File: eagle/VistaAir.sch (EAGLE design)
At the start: 10 parts

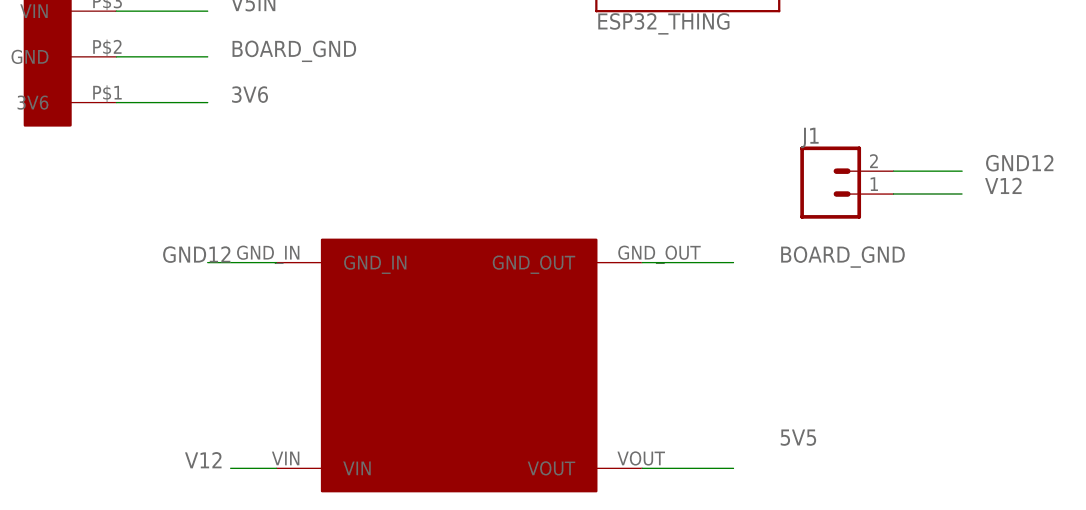
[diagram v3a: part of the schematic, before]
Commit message: proper stable power supply on board with buck converter into liner regulators
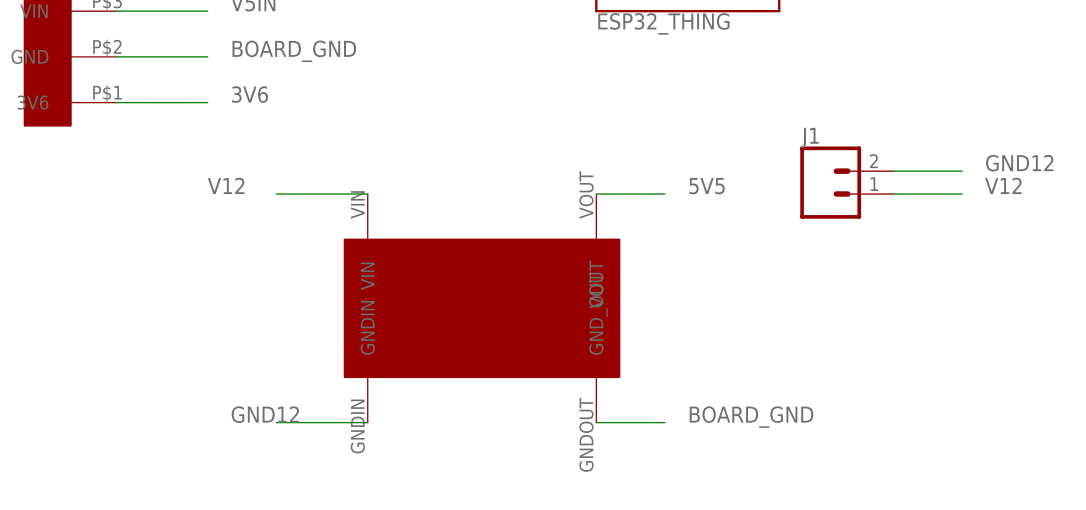
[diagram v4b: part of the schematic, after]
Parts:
- U$2: value MP1584EN_STEPDOWN_MODULE -> LM2596_STEPDOWN_MODULE; device kevins_parts:MP1584EN_STEPDOWN_MODULE -> kevins_parts:LM2596_STEPDOWN_MODULE
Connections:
- net GND12: now also U$2.GNDIN; no longer U$2.GND_IN
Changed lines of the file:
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@@
 <part name="C2" library="adafruit" deviceset="CPOL-US" device="TT5D10" value="330mu"/>
 <part name="C1" library="adafruit" deviceset="CPOL-US" device="TT2D5" value="10mu"/>
-<part name="U$2" library="kevins_parts" deviceset="MP1584EN_STEPDOWN_MODULE" device=""/>
+<part name="U$2" library="kevins_parts" deviceset="LM2596_STEPDOWN_MODULE" device=""/>
 </parts>
 <sheets>
@@
 <instance part="C2" gate="G$1" x="25.4" y="7.62"/>
 <instance part="C1" gate="G$1" x="25.4" y="40.64"/>
-<instance part="U$2" gate="G$1" x="101.6" y="-7.62"/>
+<instance part="U$2" gate="G$1" x="99.06" y="-27.94" rot="R270"/>
 </instances>
 <busses>
@@
 </segment>
 <segment>
-<pinref part="U$2" gate="G$1" pin="GND_OUT"/>
-<wire x1="121.92" y1="5.08" x2="132.08" y2="5.08" width="0.1524" layer="91"/>
-<label x="137.16" y="5.08" size="1.778" layer="95"/>
-</segment>
-<segment>
 <pinref part="L7805" gate="J$1" pin="2"/>
 <wire x1="20.32" y1="22.86" x2="25.4" y2="22.86" width="0.1524" layer="91"/>
 <label x="27.94" y="22.86" size="1.778" layer="95"/>
 </segment>
+<segment>
+<pinref part="U$2" gate="G$1" pin="GND_OUT"/>
+<wire x1="116.84" y1="-12.7" x2="124.46" y2="-12.7" width="0.1524" layer="91"/>
+<label x="127" y="-12.7" size="1.778" layer="95"/>
+</segment>
 </net>
 <net name="ENC2B" class="0">
@@
 <segment>
 <pinref part="U$2" gate="G$1" pin="VIN"/>
-<wire x1="81.28" y1="-17.78" x2="76.2" y2="-17.78" width="0.1524" layer="91"/>
-<label x="71.12" y="-17.78" size="1.778" layer="95"/>
+<wire x1="91.44" y1="12.7" x2="81.28" y2="12.7" width="0.1524" layer="91"/>
+<label x="73.66" y="12.7" size="1.778" layer="95"/>
 </segment>
 </net>
@@
 </segment>
 <segment>
-<pinref part="U$2" gate="G$1" pin="GND_IN"/>
-<wire x1="81.28" y1="5.08" x2="73.66" y2="5.08" width="0.1524" layer="91"/>
-<label x="68.58" y="5.08" size="1.778" layer="95"/>
+<pinref part="U$2" gate="G$1" pin="GNDIN"/>
+<wire x1="91.44" y1="-12.7" x2="81.28" y2="-12.7" width="0.1524" layer="91"/>
+<label x="76.2" y="-12.7" size="1.778" layer="95"/>
 </segment>
 </net>
@@
 </segment>
 <segment>
-<pinref part="U$2" gate="G$1" pin="VOUT"/>
-<wire x1="121.92" y1="-17.78" x2="132.08" y2="-17.78" width="0.1524" layer="91"/>
-<label x="137.16" y="-15.24" size="1.778" layer="95"/>
-</segment>
-<segment>
 <pinref part="L7805" gate="J$1" pin="1"/>
 <wire x1="20.32" y1="20.32" x2="25.4" y2="20.32" width="0.1524" layer="91"/>
 <label x="27.94" y="20.32" size="1.778" layer="95"/>
 </segment>
-</net>
+<segment>
+<pinref part="U$2" gate="G$1" pin="VOUT"/>
+<wire x1="116.84" y1="12.7" x2="124.46" y2="12.7" width="0.1524" layer="91"/>
+<label x="127" y="12.7" size="1.778" layer="95"/>
+</segment>
+</net>

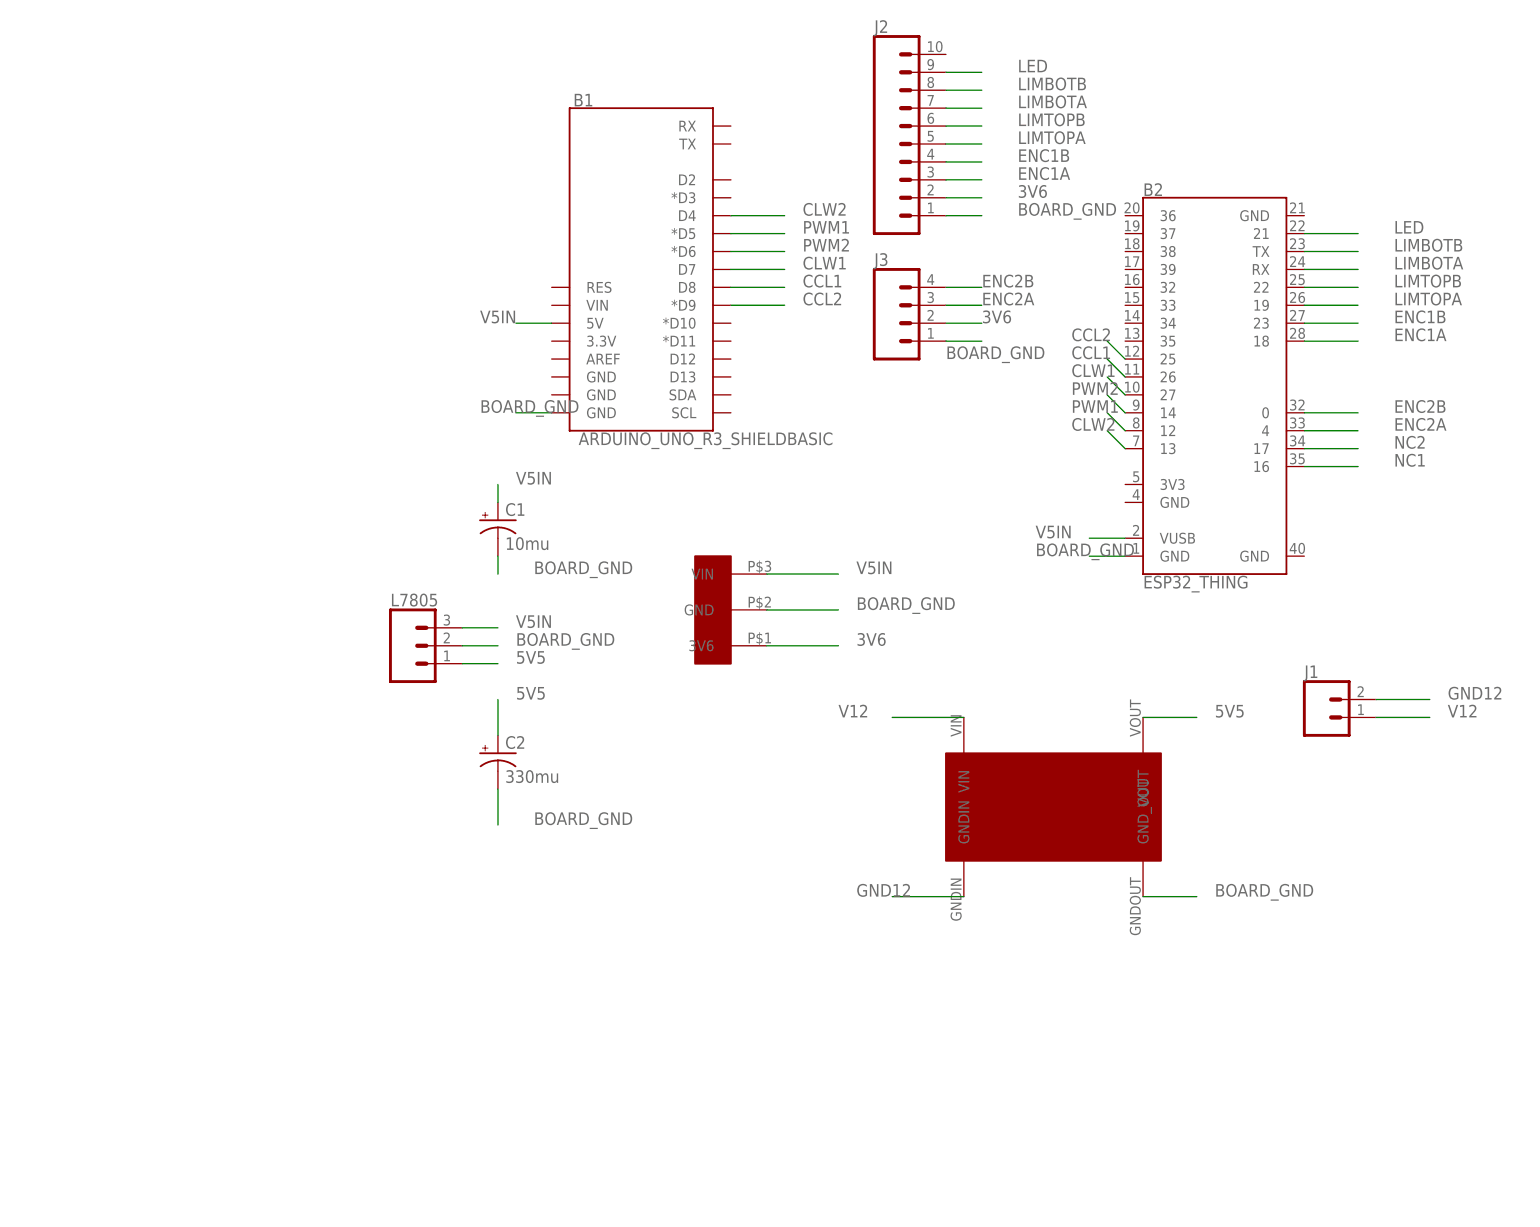
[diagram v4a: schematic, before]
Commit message: update board with logic converer from 3.3v esp32 to 5v monster moto board
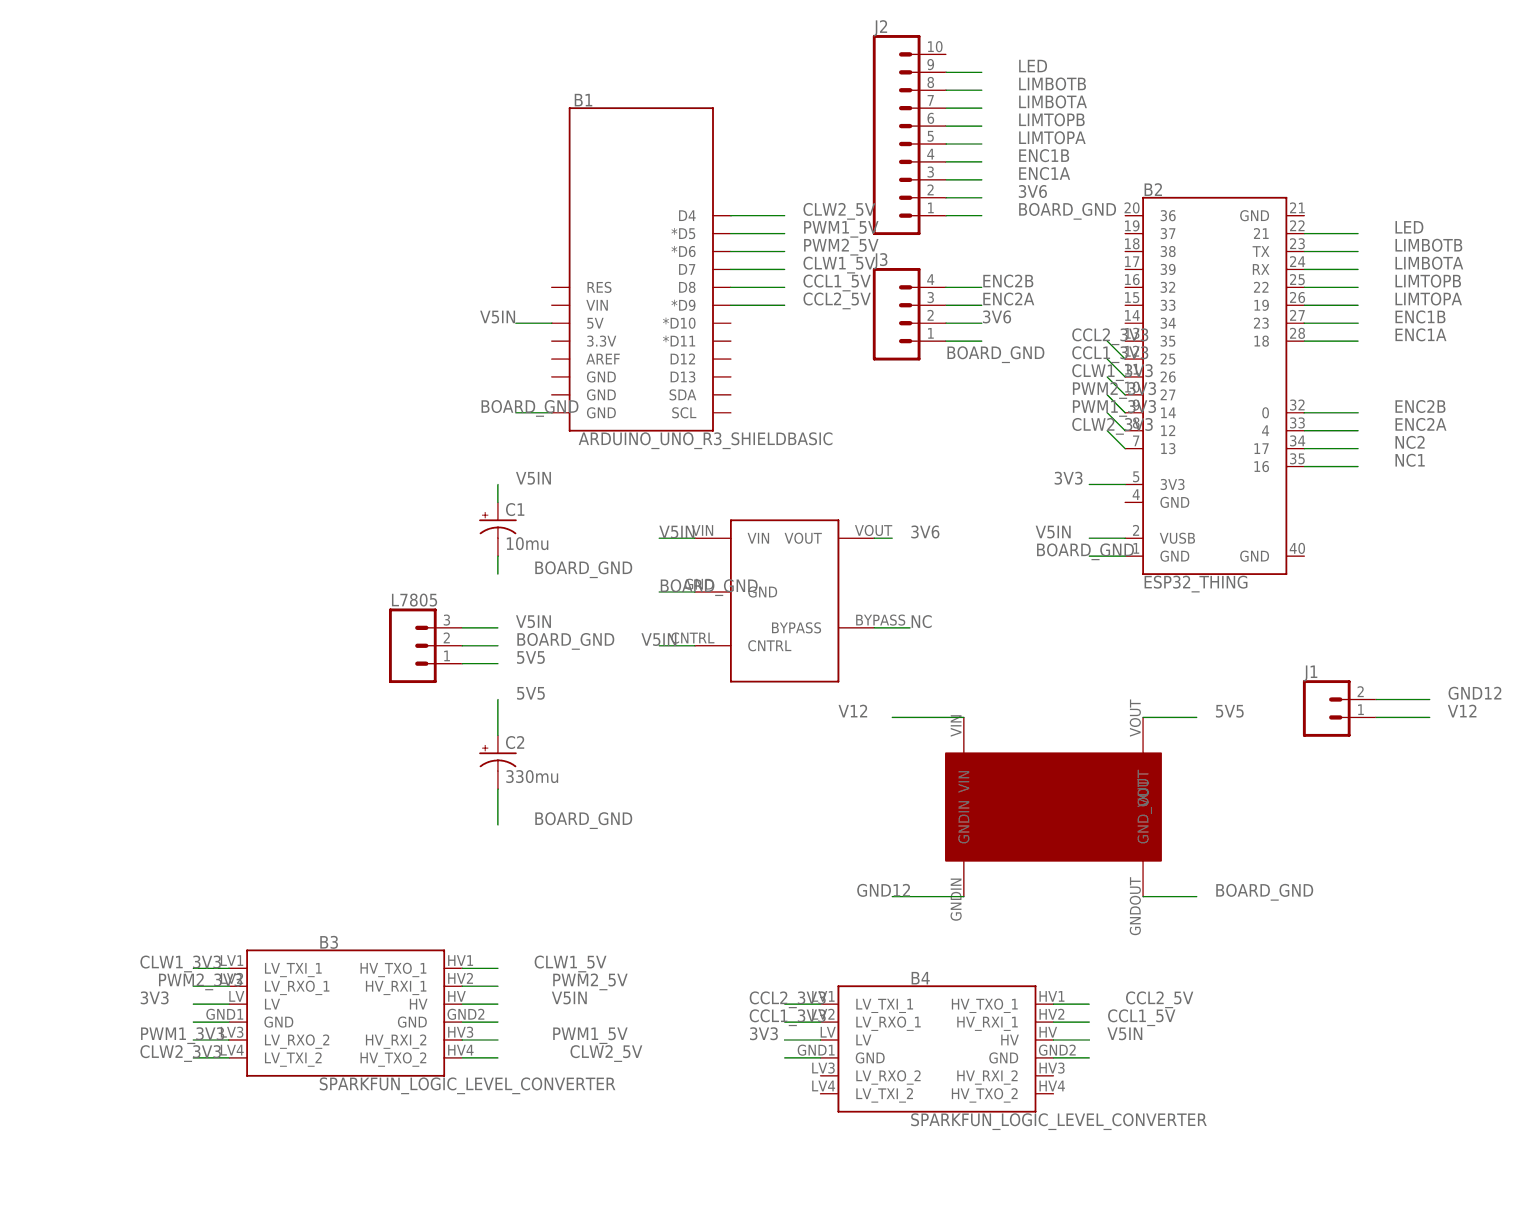
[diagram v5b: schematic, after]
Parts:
- added B3, B4: SPARKFUN_LOGIC_LEVEL_CONVERTER, SparkFun-Boards:SPARKFUN_LOGIC_LEVEL_CONVERTER
- U$1: value MCP1702_LDOREGULATOR -> LDO_REGULATOR_LP2985-N; device kevins_parts:MCP1702_LDOREGULATOR -> kevins_parts:LDO_REGULATOR_LP2985-N
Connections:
- removed net CCL1: B1.D8, B2.26
- removed net CCL2: B1.*D9, B2.25
- removed net CLW1: B1.D7, B2.27
- removed net CLW2: B1.D4, B2.13
- removed net PWM1: B1.*D5, B2.12
- removed net PWM2: B1.*D6, B2.14
- new net 3V3: B2.3V3@5, B3.LV, B4.LV
- new net CCL1_3V3: B2.26, B4.LV_RXO_1
- new net CCL1_5V: B1.D8, B4.HV_RXI_1
- new net CCL2_3V3: B2.25, B4.LV_TXI_1
- new net CCL2_5V: B1.*D9, B4.HV_TXO_1
- new net CLW1_3V3: B2.27, B3.LV_TXI_1
- new net CLW1_5V: B1.D7, B3.HV_TXO_1
- new net CLW2_3V3: B2.13, B3.LV_TXI_2
- new net CLW2_5V: B1.D4, B3.HV_TXO_2
- new net N$1: B3.GND
- new net N$2: B3.GND@2
- new net N$3: B4.GND
- new net N$4: B4.GND@2
- new net NC: U$1.BYPASS
- new net PWM1_3V3: B2.12, B3.LV_RXO_2
- new net PWM1_5V: B1.*D5, B3.HV_RXI_2
- new net PWM2_3V3: B2.14, B3.LV_RXO_1
- new net PWM2_5V: B1.*D6, B3.HV_RXI_1
- net 3V6: now also U$1.VOUT; no longer U$1.3V6
- net V5IN: now also B3.HV, B4.HV, U$1.CNTRL

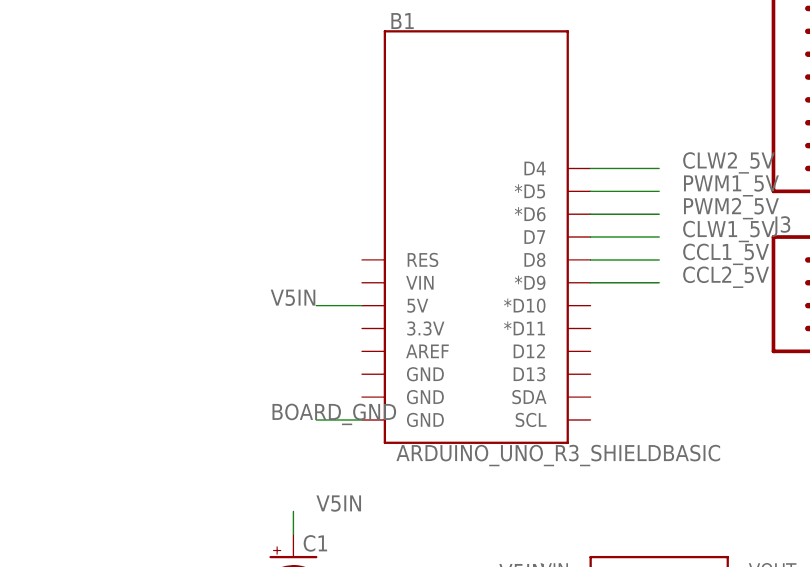
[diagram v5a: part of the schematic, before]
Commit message: managed to break ground connection to 3.6v regulator again - fixed it
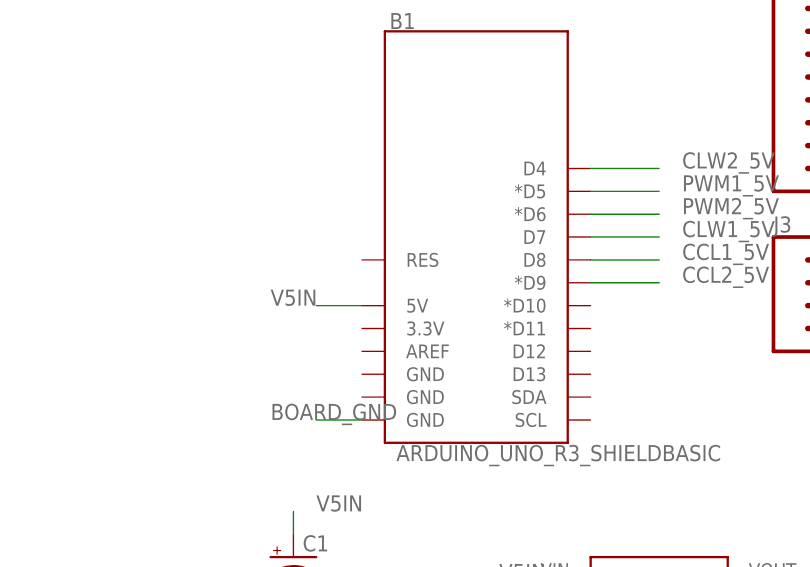
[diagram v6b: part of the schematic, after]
